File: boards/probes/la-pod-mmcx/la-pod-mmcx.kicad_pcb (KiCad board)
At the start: 4 copper layers, 73 x 21.2 mm, 16 parts, among them J1 MMCX-J-P-H-ST-EM1, J2 MMCX-J-P-H-ST-EM1, J3 MMCX-J-P-H-ST-EM1, J4 MMCX-J-P-H-ST-EM1, J5 LSHM-120-02.5-L-DV-A-N-K-TR, J6 MMCX-J-P-H-ST-EM1, J7 MMCX-J-P-H-ST-EM1, J8 MMCX-J-P-H-ST-EM1, J9 MMCX-J-P-H-ST-EM1, U1 24Cxx-DFN8

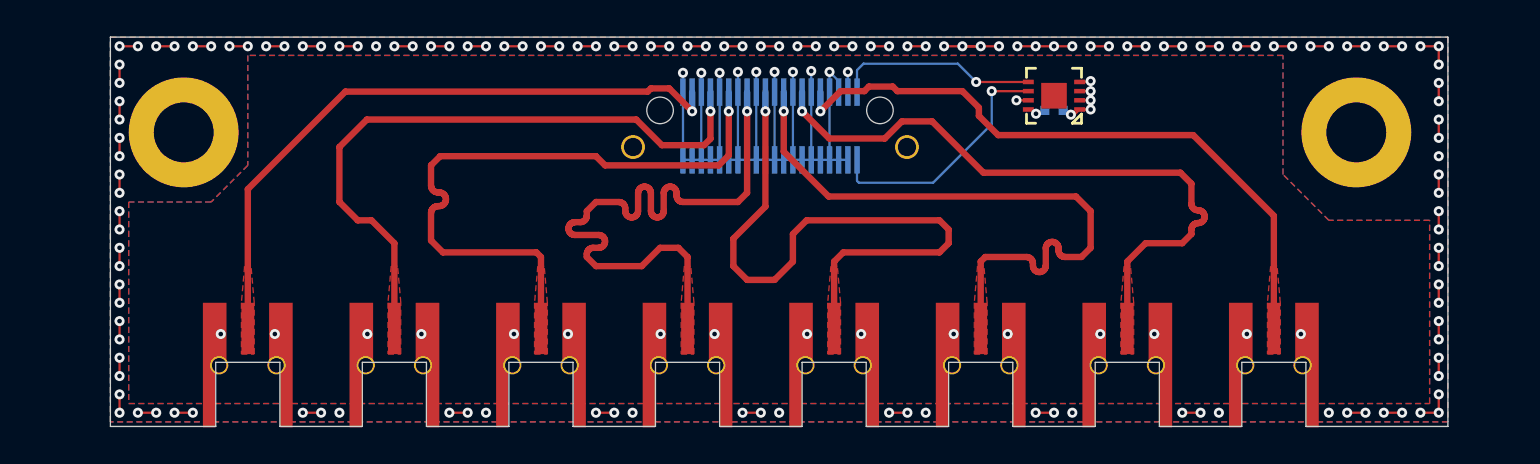
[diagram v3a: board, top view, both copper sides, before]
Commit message: Updated la-pod-mmcx with larger MMCX cutouts
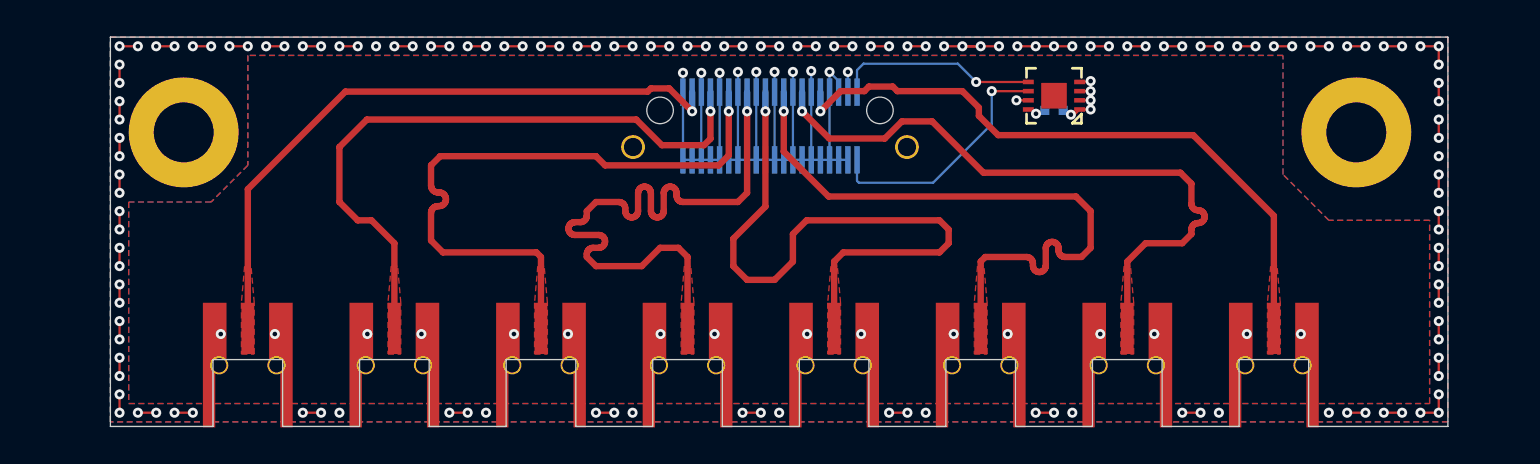
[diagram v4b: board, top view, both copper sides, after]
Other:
- outline, holes or cut-outs redrawn
- board text added: "MEAD MMCX Input Bridge A. Zonenberg / v0.2 / 2021-01-03"
- board text removed: "MEAD MMCX Input Bridge A. Zonenberg / v0.1 / 2020-06-04"
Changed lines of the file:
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@@
     )
   )
-  (gr_text "MEAD MMCX Input Bridge\nA. Zonenberg / v0.1 / 2020-06-04" (at 82 63) (layer B.SilkS)
+  (gr_text "MEAD MMCX Input Bridge\nA. Zonenberg / v0.2 / 2021-01-03" (at 82 63) (layer B.SilkS)
     (effects (font (size 0.75 0.75) (thickness 0.1)) (justify mirror))
   )
   (gr_line (start 139.5 52.5) (end 66.5 52.5) (layer Edge.Cuts) (width 0.05))
   (gr_line (start 139.5 73.75) (end 139.5 52.5) (layer Edge.Cuts) (width 0.05))
-  (gr_line (start 131.75 73.75) (end 139.5 73.75) (layer Edge.Cuts) (width 0.05))
-  (gr_line (start 131.75 70.25) (end 131.75 73.75) (layer Edge.Cuts) (width 0.05))
-  (gr_line (start 128.25 70.25) (end 131.75 70.25) (layer Edge.Cuts) (width 0.05))
-  (gr_line (start 128.25 73.75) (end 128.25 70.25) (layer Edge.Cuts) (width 0.05))
-  (gr_line (start 123.75 73.75) (end 128.25 73.75) (layer Edge.Cuts) (width 0.05))
-  (gr_line (start 123.75 70.25) (end 123.75 73.75) (layer Edge.Cuts) (width 0.05))
-  (gr_line (start 120.25 70.25) (end 123.75 70.25) (layer Edge.Cuts) (width 0.05))
-  (gr_line (start 120.25 73.75) (end 120.25 70.25) (layer Edge.Cuts) (width 0.05))
-  (gr_line (start 115.75 73.75) (end 120.25 73.75) (layer Edge.Cuts) (width 0.05))
-  (gr_line (start 115.75 70.25) (end 115.75 73.75) (layer Edge.Cuts) (width 0.05))
-  (gr_line (start 112.25 70.25) (end 115.75 70.25) (layer Edge.Cuts) (width 0.05))
-  (gr_line (start 112.25 73.75) (end 112.25 70.25) (layer Edge.Cuts) (width 0.05))
-  (gr_line (start 107.75 73.75) (end 112.25 73.75) (layer Edge.Cuts) (width 0.05))
-  (gr_line (start 107.75 70.25) (end 107.75 73.75) (layer Edge.Cuts) (width 0.05))
-  (gr_line (start 104.25 70.25) (end 107.75 70.25) (layer Edge.Cuts) (width 0.05))
-  (gr_line (start 104.25 73.75) (end 104.25 70.25) (layer Edge.Cuts) (width 0.05))
-  (gr_line (start 99.75 73.75) (end 104.25 73.75) (layer Edge.Cuts) (width 0.05))
-  (gr_line (start 99.75 70.25) (end 99.75 73.75) (layer Edge.Cuts) (width 0.05))
-  (gr_line (start 96.25 70.25) (end 99.75 70.25) (layer Edge.Cuts) (width 0.05))
-  (gr_line (start 96.25 73.75) (end 96.25 70.25) (layer Edge.Cuts) (width 0.05))
-  (gr_line (start 91.75 73.75) (end 96.25 73.75) (layer Edge.Cuts) (width 0.05))
-  (gr_line (start 91.75 70.25) (end 91.75 73.75) (layer Edge.Cuts) (width 0.05))
-  (gr_line (start 88.25 70.25) (end 91.75 70.25) (layer Edge.Cuts) (width 0.05))
-  (gr_line (start 88.25 73.75) (end 88.25 70.25) (layer Edge.Cuts) (width 0.05))
-  (gr_line (start 83.75 73.75) (end 88.25 73.75) (layer Edge.Cuts) (width 0.05))
-  (gr_line (start 83.75 70.25) (end 83.75 73.75) (layer Edge.Cuts) (width 0.05))
-  (gr_line (start 80.25 70.25) (end 83.75 70.25) (layer Edge.Cuts) (width 0.05))
-  (gr_line (start 80.25 73.75) (end 80.25 70.25) (layer Edge.Cuts) (width 0.05))
-  (gr_line (start 75.75 73.75) (end 80.25 73.75) (layer Edge.Cuts) (width 0.05))
-  (gr_line (start 75.75 70.25) (end 75.75 73.75) (layer Edge.Cuts) (width 0.05))
-  (gr_line (start 72.25 70.25) (end 75.75 70.25) (layer Edge.Cuts) (width 0.05))
-  (gr_line (start 72.25 73.75) (end 72.25 70.25) (layer Edge.Cuts) (width 0.05))
-  (gr_line (start 66.5 73.75) (end 72.25 73.75) (layer Edge.Cuts) (width 0.05))
+  (gr_line (start 131.9 73.75) (end 139.5 73.75) (layer Edge.Cuts) (width 0.05))
+  (gr_line (start 131.9 70.1) (end 131.9 73.75) (layer Edge.Cuts) (width 0.05))
+  (gr_line (start 128.1 70.1) (end 131.9 70.1) (layer Edge.Cuts) (width 0.05))
+  (gr_line (start 128.1 73.75) (end 128.1 70.1) (layer Edge.Cuts) (width 0.05))
+  (gr_line (start 123.9 73.75) (end 128.1 73.75) (layer Edge.Cuts) (width 0.05))
+  (gr_line (start 123.9 70.1) (end 123.9 73.75) (layer Edge.Cuts) (width 0.05))
+  (gr_line (start 120.1 70.1) (end 123.9 70.1) (layer Edge.Cuts) (width 0.05))
+  (gr_line (start 120.1 73.75) (end 120.1 70.1) (layer Edge.Cuts) (width 0.05))
+  (gr_line (start 115.9 73.75) (end 120.1 73.75) (layer Edge.Cuts) (width 0.05))
+  (gr_line (start 115.9 70.1) (end 115.9 73.75) (layer Edge.Cuts) (width 0.05))
+  (gr_line (start 112.1 70.1) (end 115.9 70.1) (layer Edge.Cuts) (width 0.05))
+  (gr_line (start 112.1 73.75) (end 112.1 70.1) (layer Edge.Cuts) (width 0.05))
+  (gr_line (start 107.9 73.75) (end 112.1 73.75) (layer Edge.Cuts) (width 0.05))
+  (gr_line (start 107.9 70.1) (end 107.9 73.75) (layer Edge.Cuts) (width 0.05))
+  (gr_line (start 104.1 70.1) (end 107.9 70.1) (layer Edge.Cuts) (width 0.05))
+  (gr_line (start 104.1 73.75) (end 104.1 70.1) (layer Edge.Cuts) (width 0.05))
+  (gr_line (start 99.9 73.75) (end 104.1 73.75) (layer Edge.Cuts) (width 0.05))
+  (gr_line (start 99.9 70.1) (end 99.9 73.75) (layer Edge.Cuts) (width 0.05))
+  (gr_line (start 96.1 70.1) (end 99.9 70.1) (layer Edge.Cuts) (width 0.05))
+  (gr_line (start 96.1 73.75) (end 96.1 70.1) (layer Edge.Cuts) (width 0.05))
+  (gr_line (start 91.9 73.75) (end 96.1 73.75) (layer Edge.Cuts) (width 0.05))
+  (gr_line (start 91.9 70.1) (end 91.9 73.75) (layer Edge.Cuts) (width 0.05))
+  (gr_line (start 88.1 70.1) (end 91.9 70.1) (layer Edge.Cuts) (width 0.05))
+  (gr_line (start 88.1 73.75) (end 88.1 70.1) (layer Edge.Cuts) (width 0.05))
+  (gr_line (start 83.9 73.75) (end 88.1 73.75) (layer Edge.Cuts) (width 0.05))
+  (gr_line (start 83.9 70.1) (end 83.9 73.75) (layer Edge.Cuts) (width 0.05))
+  (gr_line (start 80.1 70.1) (end 83.9 70.1) (layer Edge.Cuts) (width 0.05))
+  (gr_line (start 80.1 73.75) (end 80.1 70.1) (layer Edge.Cuts) (width 0.05))
+  (gr_line (start 75.9 73.75) (end 80.1 73.75) (layer Edge.Cuts) (width 0.05))
+  (gr_line (start 75.9 70.1) (end 75.9 73.75) (layer Edge.Cuts) (width 0.05))
+  (gr_line (start 72.1 70.1) (end 75.9 70.1) (layer Edge.Cuts) (width 0.05))
+  (gr_line (start 72.1 73.75) (end 72.1 70.1) (layer Edge.Cuts) (width 0.05))
+  (gr_line (start 66.5 73.75) (end 72.1 73.75) (layer Edge.Cuts) (width 0.05))
   (gr_line (start 66.5 52.5) (end 66.5 73.75) (layer Edge.Cuts) (width 0.05))
   (via (at 131.475 68.705) (size 0.55) (drill 0.25) (layers F.Cu B.Cu) (net 1))
